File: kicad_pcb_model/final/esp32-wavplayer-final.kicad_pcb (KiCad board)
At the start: 2 copper layers, 29 x 37 mm, 115 parts, among them J3 DBG3v3, SW1 RST, SW2 BOOT/UP, SW3 RIGHT, SW4 LEFT, SW5 DOWN, U3 PCM5102A

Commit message: screen
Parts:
- BB1, BCC1, BCC2, BCC3, BCL1, BCR1, BCR2, DB2, DB4, DC1, DC3, DC4, DC5, DC6, DC7, DQ1, DQ2, DR1, DR2, DR3, DR4, DR5, DS1: moved to B.Cu
- moved DQ1 102.8 mm to (264.7, 56.2), turned to 180 degrees
- moved DQ2 102.8 mm to (264.7, 60.6), turned to 180 degrees
- moved DB2 101.1 mm to (263.7, 73.5)
- moved DR5 94.2 mm to (259.5, 60.2), turned to 180 degrees
- moved DR4 88.2 mm to (255.8, 60.2), turned to 180 degrees
- moved DB4 81.9 mm to (251.6, 73.2), turned to 180 degrees
- moved DR2 52.2 mm to (235.1, 108.8), turned to 180 degrees
- moved DS1 49.1 mm to (233.8, 103.8), turned to 180 degrees
- moved BCC1 45.9 mm to (238.8, 113.3), turned to 180 degrees
- moved BCC2 45.9 mm to (238.8, 115.8), turned to 180 degrees
- moved DC5 44.8 mm to (243.2, 107.4), turned to -90 degrees
- moved DR1 44.6 mm to (235.1, 110.3), turned to 180 degrees
- moved DC3 44.3 mm to (238.5, 108.1)
- moved DC6 43.5 mm to (241.4, 107.4), turned to -90 degrees
- moved DR3 41.9 mm to (228.2, 107.2), turned to 90 degrees
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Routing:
- net Earth: track 156.1 -> 202.8 mm
- net /GPIO8: track 1.60 -> 10.3 mm
- net +3V3: track 72.2 -> 80.2 mm
- net /GPIO9: track 0.00 -> 5.27 mm
- net Net-(DS1-C1N): track 0.00 -> 4.99 mm
- net Net-(DS1-C2P): track 0.00 -> 4.85 mm
- net Net-(DS1-IREF): track 0.00 -> 3.43 mm
- net Net-(DS1-C1P): track 0.00 -> 2.92 mm
- net Net-(DS1-VCOMH): track 0.00 -> 2.89 mm
- net Net-(DS1-C2N): track 0.00 -> 2.77 mm
- net Net-(DS1-VCC): track 0.00 -> 2.29 mm
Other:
- board size 29 x 37 mm -> 54 x 37 mm

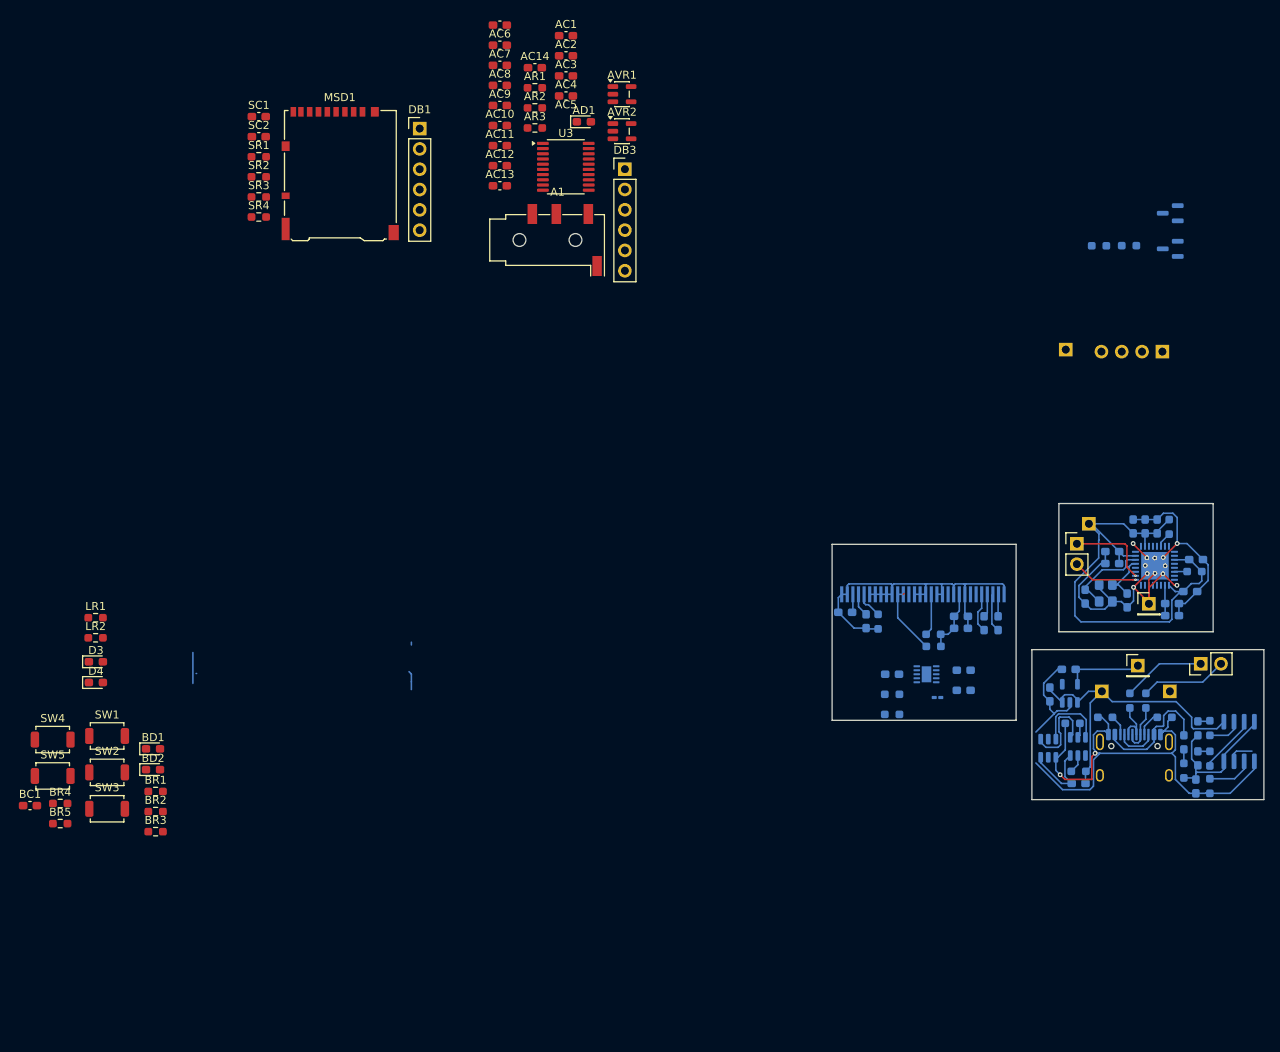
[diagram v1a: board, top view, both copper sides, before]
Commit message: finished screen, added sdcard
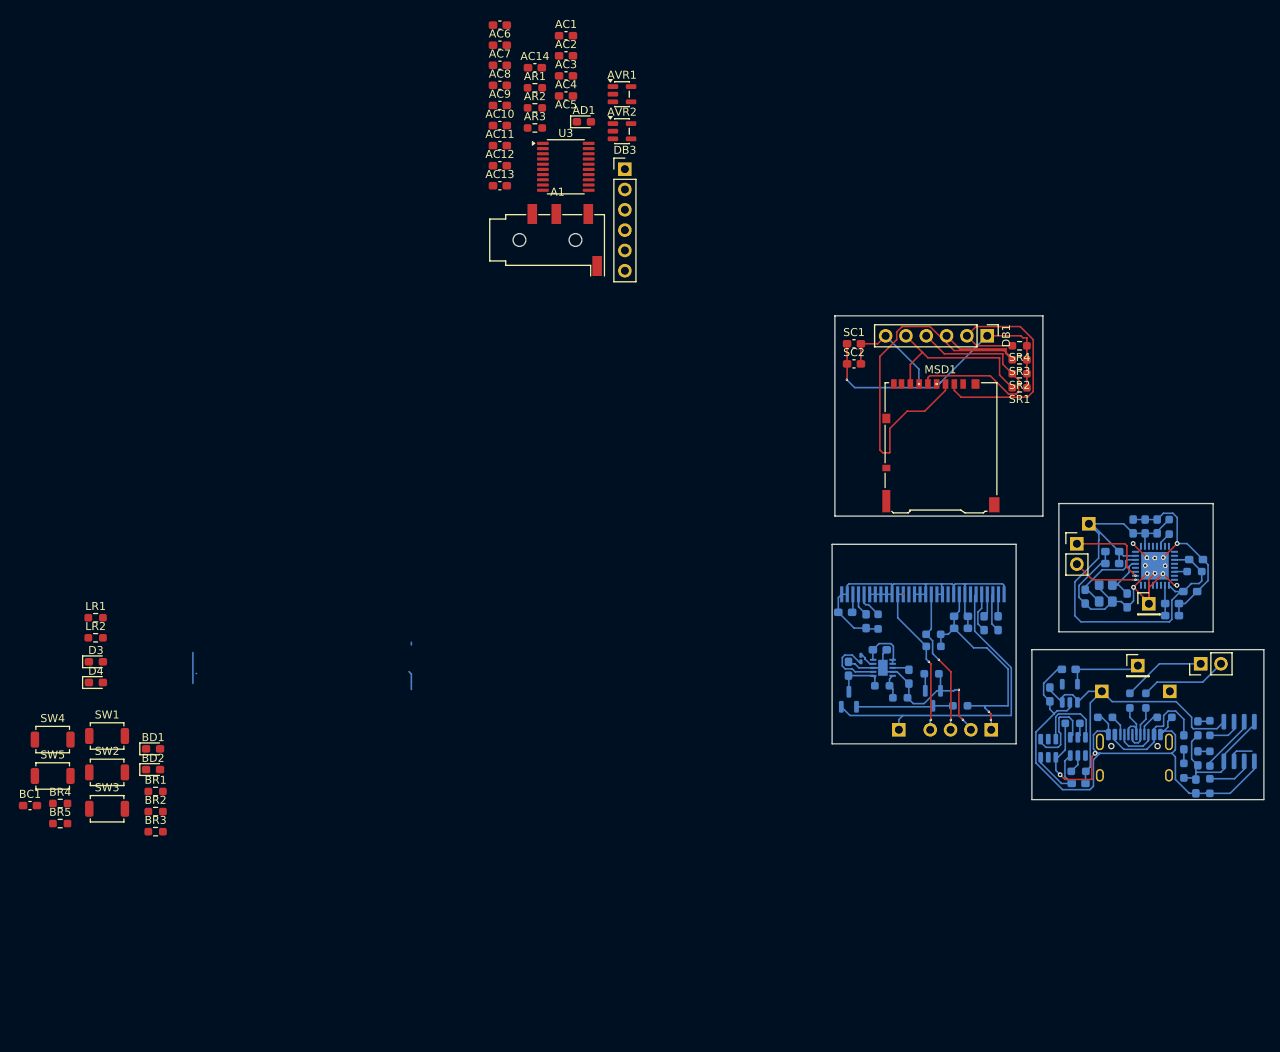
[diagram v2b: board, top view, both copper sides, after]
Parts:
- moved SR1 99.4 mm to (245.8, 78.0), turned to 180 degrees
- moved SR2 98.2 mm to (245.8, 76.2), turned to 180 degrees
- moved SR3 97.3 mm to (245.8, 74.5), turned to 180 degrees
- moved SR4 96.5 mm to (245.8, 72.8), turned to 180 degrees
- moved MSD1 82.4 mm to (236.0, 85.2)
- moved SC1 79.6 mm to (225.1, 72.5)
- moved SC2 79.6 mm to (225.1, 75.0)
- moved DB1 75.5 mm to (241.8, 71.5), turned to -90 degrees
- moved DQ1 72.8 mm to (224.5, 116.9), turned to 90 degrees
- moved DQ2 63.5 mm to (235.0, 116.8), turned to -90 degrees
- moved DR4 60.1 mm to (238.4, 117.8), turned to 0 degrees
- moved DR5 58.9 mm to (234.8, 113.8), turned to 0 degrees
- moved DB4 51.9 mm to (230.8, 120.8)
- moved DB2 51.9 mm to (242.3, 120.8)
- moved BCC2 11.6 mm to (228.4, 110.8)
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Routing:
- net +3V3: track 80.2 -> 145.7 mm, vias 0 -> 4
- net /GPIO6: track 0.00 -> 56.1 mm
- net Earth: track 202.8 -> 249.2 mm, vias 14 -> 17
- net /VBAT: track 0.00 -> 40.8 mm
- net /GPIO7: track 0.00 -> 33.4 mm
- net /GPIO4: track 0.00 -> 29.3 mm
- net /GPIO5: track 0.00 -> 21.8 mm
- net /GPIO9: track 5.27 -> 18.5 mm, vias 0 -> 2
- net Net-(DQ1-G): track 0.00 -> 12.1 mm
- net /GPIO8: track 10.3 -> 21.0 mm, vias 0 -> 2
- net Net-(BB1-L2): track 0.00 -> 8.02 mm
- net /BATT: track 0.00 -> 6.48 mm
- net Net-(BB1-FB): track 0.00 -> 3.09 mm
- net /GPIO: track 0.00 -> 2.18 mm
- net Net-(BB1-VINA): track 0.00 -> 2.14 mm
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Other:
- board size 54 x 37 mm -> 54 x 60.5 mm

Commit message: Generating debug files
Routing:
- net Net-(BATPROT1-GND): track 10.5 -> 35.3 mm, vias 0 -> 1
- net Earth: track 249.2 -> 250.6 mm
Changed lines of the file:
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@@
 			(outputformat 1)
 			(mirror no)
-			(drillshape 1)
+			(drillshape 0)
 			(scaleselection 1)
-			(outputdirectory "")
+			(outputdirectory "ESP32-Debug/")
 		)
 	)
@@
 		(tags "resistor handsolder")
 		(property "Reference" "SR2"
-			(at 0 -1.43 0)
+			(at -0.1625 -7.25 0)
 			(layer "F.SilkS")
 			(effects
@@
 		(tags "Through hole pin header THT 1x06 2.54mm single row")
 		(property "Reference" "DB1"
-			(at 0 -2.38 90)
+			(at -0.75 -2.38 90)
 			(layer "F.SilkS")
 			(effects
@@
 		(tags "resistor handsolder")
 		(property "Reference" "SR4"
-			(at 0 -1.43 0)
+			(at -0.1625 -7.25 0)
 			(layer "F.SilkS")
 			(effects
@@
 		(tags "resistor handsolder")
 		(property "Reference" "SR3"
-			(at 0 -1.43 0)
+			(at -0.1625 -7.25 0)
 			(layer "F.SilkS")
 			(effects
@@
 		(tags "resistor handsolder")
 		(property "Reference" "SR1"
-			(at 0 -1.43 0)
+			(at -0.1625 -7.25 0)
 			(layer "F.SilkS")
 			(effects
@@
 		(tags "capacitor handsolder")
 		(property "Reference" "SC2"
-			(at 0 -1.43 0)
+			(at 0 1.49 0)
 			(layer "F.SilkS")
 			(effects
@@
 		(tags "capacitor handsolder")
 		(property "Reference" "DC7"
-			(at 0 1.43 90)
+			(at -1.075 -1.15 90)
 			(layer "B.SilkS")
 			(effects
@@
 		(tags "capacitor handsolder")
 		(property "Reference" "DC3"
-			(at 0 1.43 0)
+			(at -0.0125 1.9375 0)
 			(layer "B.SilkS")
 			(effects
@@
 		(tags "SOT TO_SOT_SMD")
 		(property "Reference" "DQ2"
-			(at 0 2.4 90)
+			(at -1.0625 -2.25 90)
 			(layer "B.SilkS")
 			(effects
@@
 		(tags "inductor handsolder")
 		(property "Reference" "BCL1"
-			(at 0 1.05 90)
+			(at -1.3425 1.05 180)
 			(layer "B.SilkS")
 			(effects
@@
 		(tags "SOT TO_SOT_SMD")
 		(property "Reference" "DQ1"
-			(at 0 2.4 90)
+			(at -3.0625 0 180)
 			(layer "B.SilkS")
 			(effects
@@
 		(tags "capacitor handsolder")
 		(property "Reference" "BCC1"
-			(at 0 1.43 90)
+			(at 0 1.25 90)
 			(layer "B.SilkS")
 			(effects
@@
 			(at 0 2.38 0)
 			(layer "B.SilkS")
+			(hide yes)
 			(effects
 				(font
@@
 		(tags "capacitor handsolder")
 		(property "Reference" "DC5"
-			(at 0 1.43 90)
+			(at 0.075 -1.35 90)
 			(layer "B.SilkS")
 			(effects
@@
 		(tags "resistor handsolder")
 		(property "Reference" "DR1"
-			(at 0 1.43 0)
+			(at 0.0875 -1.4275 0)
 			(layer "B.SilkS")
 			(effects
@@
 		(tags "resistor handsolder")
 		(property "Reference" "BCR2"
-			(at 0 1.43 0)
+			(at 0.0875 1.75 0)
 			(layer "B.SilkS")
 			(effects
@@
 		(tags "resistor handsolder")
 		(property "Reference" "DR2"
-			(at -0.1625 1.5 0)
+			(at 0.0625 1.3125 0)
 			(layer "B.SilkS")
 			(effects
@@
 		(tags "resistor handsolder")
 		(property "Reference" "DR5"
-			(at 0 1.43 0)
+			(at 2.1625 -1 90)
 			(layer "B.SilkS")
 			(effects
@@
 		(tags "resistor handsolder")
 		(property "Reference" "BCR1"
-			(at 0 1.43 0)
+			(at -1.1625 1.43 180)
 			(layer "B.SilkS")
 			(effects
@@
 		(tags "display oled")
 		(property "Reference" "DS1"
-			(at -0.35 -2.1 0)
+			(at -0.75 1.0625 0)
 			(layer "B.SilkS")
+			(hide yes)
 			(effects
 				(font
@@
 		(tags "capacitor handsolder")
 		(property "Reference" "DC4"
-			(at 0 1.43 0)
+			(at 0 1.0625 0)
 			(layer "B.SilkS")
 			(effects
@@
 		(tags "capacitor handsolder")
 		(property "Reference" "DC1"
-			(at 0 1.43 0)
+			(at 0 1.43 90)
 			(layer "B.SilkS")
 			(effects
@@
 		(tags "capacitor handsolder")
 		(property "Reference" "DC6"
-			(at 0 1.43 90)
+			(at 2.325 -0.1 180)
 			(layer "B.SilkS")
 			(effects
@@
 	)
 	(segment
+		(start 274.881249 123.41625)
+		(end 275.18125 123.716251)
+		(width 0.2)
+		(layer "B.Cu")
+		(net "Earth")
+	)
+	(segment
 		(start 265.31125 124.13125)
 		(end 264.87125 123.69125)
@@
 	)
 	(segment
+		(start 275.18125 123.716251)
+		(end 275.18125 124.69125)
+		(width 0.2)
+		(layer "B.Cu")
+		(net "Earth")
+	)
+	(segment
 		(start 229.9 103.8125)
 		(end 229.9 102.7125)
@@
 	)
 	(segment
+		(start 265.31125 116.63125)
+		(end 265.31125 127.43875)
+		(width 0.2)
+		(layer "F.Cu")
+		(net "Net-(BATPROT1-GND)")
+	)
+	(segment
+		(start 265.20875 127.54125)
+		(end 252.433924 127.54125)
+		(width 0.2)
+		(layer "F.Cu")
+		(net "Net-(BATPROT1-GND)")
+	)
+	(segment
+		(start 264.62125 115.94125)
+		(end 265.31125 116.63125)
+		(width 0.2)
+		(layer "F.Cu")
+		(net "Net-(BATPROT1-GND)")
+	)
+	(segment
+		(start 252.433924 127.54125)
+		(end 252.350485 127.457811)
+		(width 0.2)
+		(layer "F.Cu")
+		(net "Net-(BATPROT1-GND)")
+	)
+	(segment
+		(start 265.31125 127.43875)
+		(end 265.20875 127.54125)
+		(width 0.2)
+		(layer "F.Cu")
+		(net "Net-(BATPROT1-GND)")
+	)
+	(via micro
+		(at 252.350485 127.457811)
+		(size 0.3)
+		(drill 0.1)
+		(layers "F.Cu" "B.Cu")
+		(net "Net-(BATPROT1-GND)")
+	)
+	(segment

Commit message: Swapped microvias for throughvias
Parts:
- moved BTM1 29.6 mm to (267.4, 151.2)
- moved PR2 29.6 mm to (258.1, 148.2)
- moved REF** 29.6 mm to (262.6, 141.5)
- moved PDVR1 29.6 mm to (246.2, 145.2)
- moved PR1 29.6 mm to (250.7, 148.2)
- moved PR7 29.6 mm to (247.3, 155.0)
- moved PR8 29.6 mm to (246.6, 149.0)
- moved + 29.6 mm to (250.2, 145.0)
- moved - 29.6 mm to (258.8, 145.0)
- moved D5 29.6 mm to (262.2, 153.3)
- moved D6 29.6 mm to (262.2, 149.6)
- moved PC2 29.6 mm to (246.1, 142.2)
- moved PD1 29.6 mm to (260.5, 151.3)
- moved PR4 29.6 mm to (263.8, 149.6)
- moved PR6 29.6 mm to (263.8, 156.8)
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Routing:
- net Earth: track 250.6 -> 244.4 mm
- net /XTAL_N: track 6.71 -> 7.80 mm
- net +3V3: track 145.7 -> 146.7 mm
- net /GPIO18/USB_D+: track 20.9 -> 21.9 mm
- net /GPIO19/USB_D-: track 19.1 -> 19.6 mm
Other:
- board size 54 x 60.5 mm -> 48.1 x 90 mm
